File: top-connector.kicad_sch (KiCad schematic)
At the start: 6 parts, among them J1 Compute-Module-4_Plug_Connect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, Q2 PJE138K

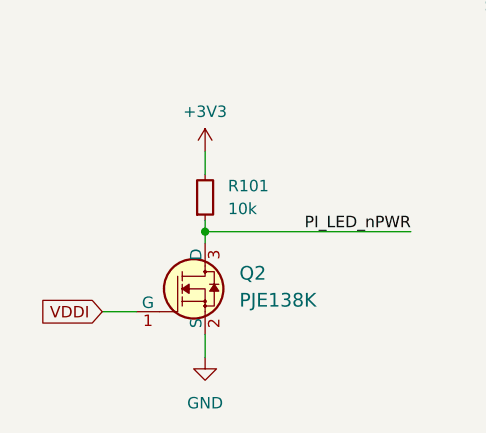
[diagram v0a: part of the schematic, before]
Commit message: [#57505] Continue migration to hierarchical schematic
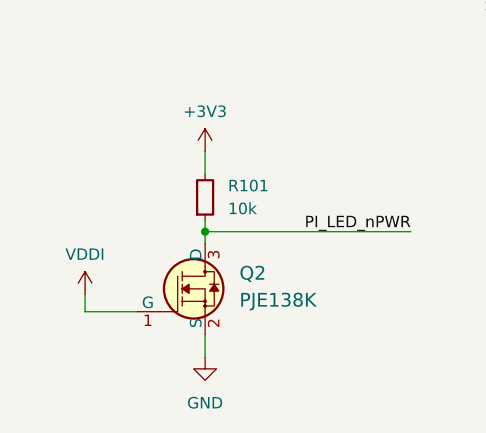
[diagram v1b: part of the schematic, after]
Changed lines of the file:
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@@
+    (stroke (width 0) (type default))
+  )
+  (wire (pts (xy 33.655 156.845) (xy 33.655 158.75))
     (stroke (width 0) (type default))
   )
@@
     (stroke (width 0) (type default))
   )
-  (wire (pts (xy 35.56 158.75) (xy 39.37 158.75))
+  (wire (pts (xy 33.655 158.75) (xy 39.37 158.75))
     (stroke (width 0) (type default))
   )
@@
     (effects (font (size 1.27 1.27)) (justify right))
     (property "Intersheetrefs" "${INTERSHEET_REFS}" (at 96.0421 76.1206 0)
-      (effects (font (size 1.27 1.27)) (justify right))
-    )
-  )
-  (global_label "VDDI" (shape input) (at 35.56 158.75 180) (fields_autoplaced)
-    (effects (font (size 1.27 1.27)) (justify right))
-    (property "Intersheetrefs" "${INTERSHEET_REFS}" (at 28.3414 158.75 0)
       (effects (font (size 1.27 1.27)) (justify right))
     )
@@
         )
       )
+    )
+  )
+  (symbol (lib_id "antmicropower:VDDI") (at 33.655 156.845 0) (unit 1)
+    (in_bom yes) (on_board yes) (dnp no) (fields_autoplaced)
+    (property "Reference" "#PWR0323" (at 33.655 160.655 0)
+      (effects (font (size 1.27 1.27)) hide)
+    )
+    (property "Value" "VDDI" (at 33.655 152.4 0)
+      (effects (font (size 1.27 1.27)))
+    )
+    (property "Footprint" "" (at 33.655 156.845 0)
+      (effects (font (size 1.27 1.27)) hide)
+    )
+    (property "Datasheet" "" (at 33.655 156.845 0)
+      (effects (font (size 1.27 1.27)) hide)
+    )
+    (pin "1")
+    (instances
+      (project "polarfire-som"
+        (path "/db4a0d3e-2eb3-499e-977d-6eb378cfd3ed/debae449-a92d-4184-817e-09f6daf3da7c"
+          (reference "#PWR0323") (unit 1)
+        )
+      )

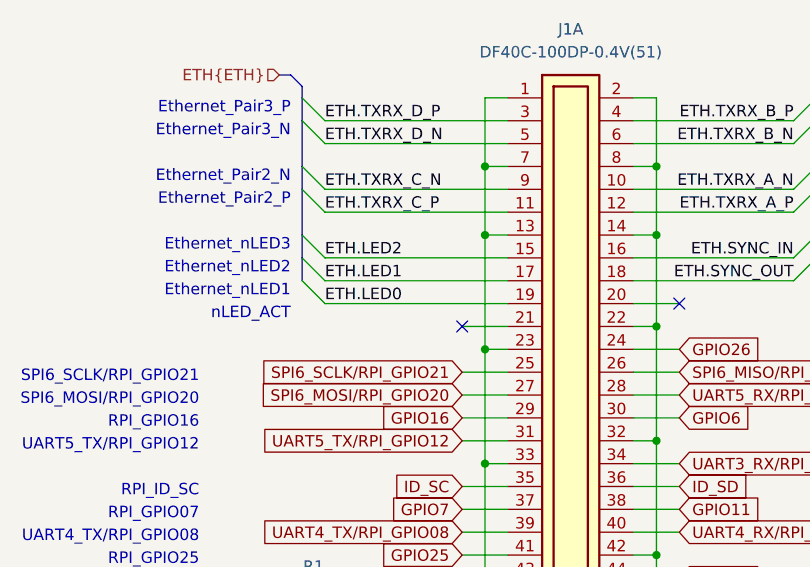
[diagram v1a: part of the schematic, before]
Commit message: [#57422] Add ETH PHY strap, WL_BT UART level shifter, fiducials, remove BYP_EN
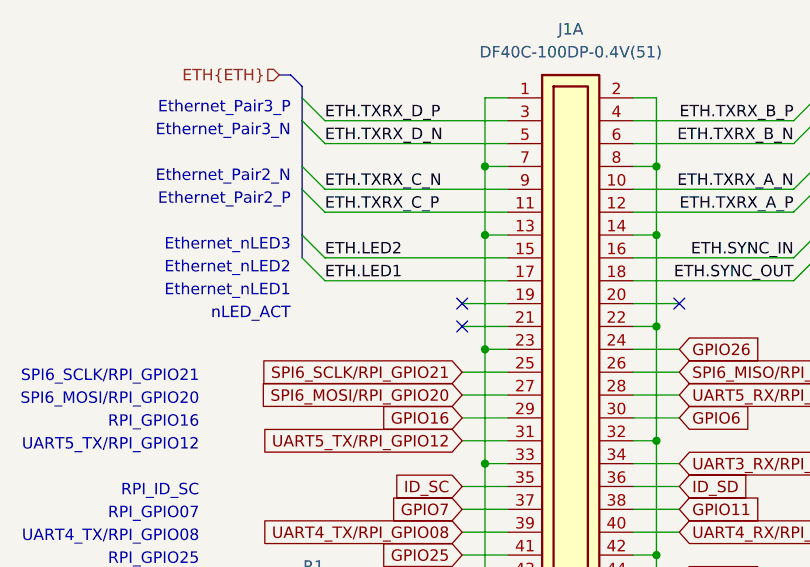
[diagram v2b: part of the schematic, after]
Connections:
- net ETH.LED0: no longer names the net of J1.19
- no-connect marks 9 -> 10
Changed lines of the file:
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@@
   (no_connect (at 104.14 55.88))
   (no_connect (at 123.19 124.46))
+  (no_connect (at 104.14 53.34))
   (no_connect (at 123.19 154.94))
   (no_connect (at 128.27 53.34))
@@
     (stroke (width 0) (type default))
   )
-  (bus_entry (at 86.36 50.8) (size 2.54 2.54)
-    (stroke (width 0) (type default))
-  )
   (bus_entry (at 41.148 99.06) (size 2.54 2.54)
     (stroke (width 0) (type default))
@@
     (stroke (width 0) (type default))
   )
+  (wire (pts (xy 104.14 53.34) (xy 109.22 53.34))
+    (stroke (width 0) (type default))
+  )
   (wire (pts (xy 104.14 63.5) (xy 109.22 63.5))
     (stroke (width 0) (type default))
@@
     (stroke (width 0) (type default))
   )
-  (bus (pts (xy 86.36 48.26) (xy 86.36 50.8))
-    (stroke (width 0) (type default))
-  )
   (wire (pts (xy 106.68 45.72) (xy 106.68 58.42))
     (stroke (width 0) (type default))
@@
     (stroke (width 0) (type default))
   )
-  (wire (pts (xy 88.9 53.34) (xy 109.22 53.34))
-    (stroke (width 0) (type default))
-  )
   (wire (pts (xy 104.14 133.35) (xy 104.14 134.62))
     (stroke (width 0) (type default))
@@
     (effects (font (size 1.27 1.27)) (justify right bottom))
   )
-  (label "ETH.LED0" (at 88.9 53.34 0) (fields_autoplaced)
-    (effects (font (size 1.27 1.27)) (justify left bottom))
-  )
   (label "ETH.LED1" (at 88.9 50.8 0) (fields_autoplaced)

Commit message: [#57505] Finish defining buses
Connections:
- net ID_SC renamed ID.SCL
- net ID_SD renamed ID.SDA
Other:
- moved on the sheet: J1A, Q2, R1, R101, R13, R15

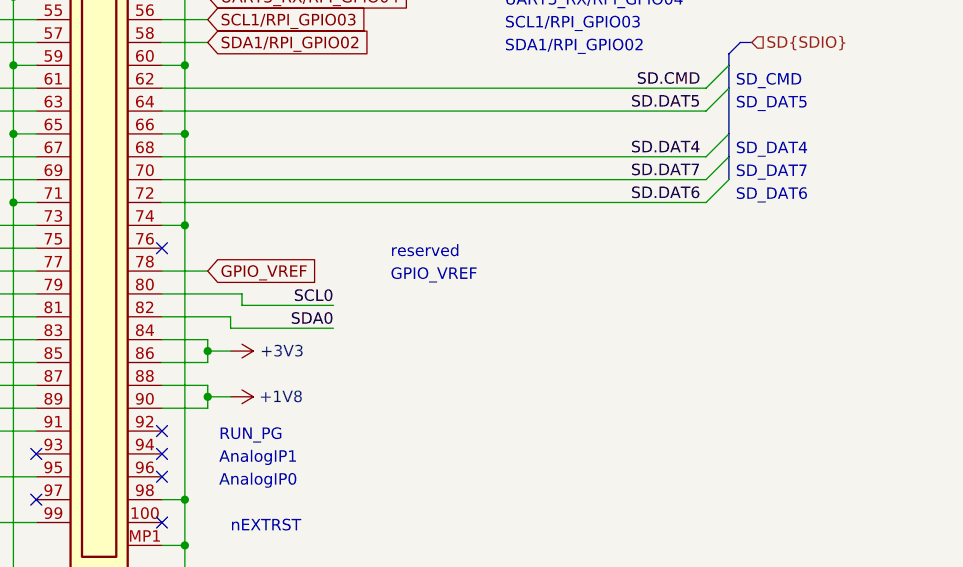
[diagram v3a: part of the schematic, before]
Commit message: [#57505] Start moving logic level converters to GPIO sheet
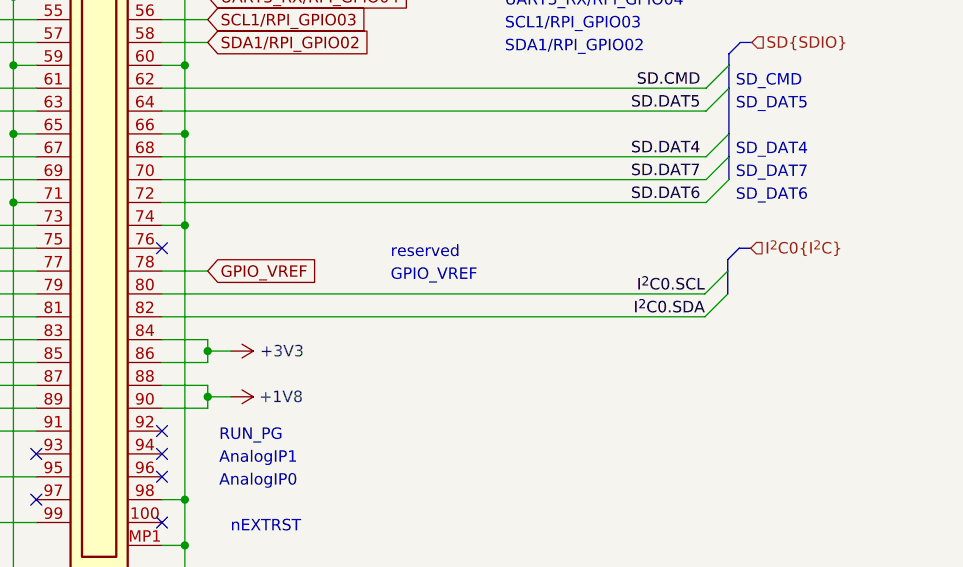
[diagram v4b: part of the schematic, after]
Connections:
- net SCL0 renamed I^{2}C0.SCL
- net SDA0 renamed I^{2}C0.SDA
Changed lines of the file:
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@@
+    (stroke (width 0) (type default))
+  )
+  (bus_entry (at 277.495 175.895) (size -2.54 2.54)
     (stroke (width 0) (type default))
   )
@@
     (stroke (width 0) (type default))
   )
+  (bus_entry (at 277.495 173.355) (size -2.54 2.54)
+    (stroke (width 0) (type default))
+  )
   (bus (pts (xy 177.8 92.075) (xy 177.8 94.615))
     (stroke (width 0) (type default))
@@
     (stroke (width 0) (type default))
   )
+  (bus (pts (xy 280.035 170.815) (xy 278.765 170.815))
+    (stroke (width 0) (type default))
+  )
   (wire (pts (xy 214.63 99.695) (xy 219.71 99.695))
     (stroke (width 0) (type default))
@@
     (stroke (width 0) (type default))
   )
-  (wire (pts (xy 222.25 179.705) (xy 233.68 179.705))
-    (stroke (width 0) (type default))
-  )
   (wire (pts (xy 195.58 186.055) (xy 200.66 186.055))
     (stroke (width 0) (type default))
@@
     (stroke (width 0) (type default))
   )
-  (wire (pts (xy 223.52 177.165) (xy 223.52 175.895))
-    (stroke (width 0) (type default))
-  )
   (wire (pts (xy 195.58 188.595) (xy 200.66 188.595))
     (stroke (width 0) (type default))
@@
     (stroke (width 0) (type default))
   )
-  (wire (pts (xy 223.52 175.895) (xy 214.63 175.895))
+  (wire (pts (xy 214.63 175.895) (xy 274.955 175.895))
     (stroke (width 0) (type default))
   )
@@
     (stroke (width 0) (type default))
   )
-  (wire (pts (xy 223.52 177.165) (xy 233.68 177.165))
-    (stroke (width 0) (type default))
-  )
   (bus (pts (xy 234.95 92.075) (xy 234.95 94.615))
     (stroke (width 0) (type default))
   )
+  (bus (pts (xy 277.495 172.085) (xy 277.495 173.355))
+    (stroke (width 0) (type default))
+  )
   (wire (pts (xy 219.71 187.325) (xy 219.71 186.055))
     (stroke (width 0) (type default))
@@
     (stroke (width 0) (type default))
   )
-  (wire (pts (xy 222.25 179.705) (xy 222.25 178.435))
-    (stroke (width 0) (type default))
-  )
   (wire (pts (xy 200.66 76.835) (xy 198.12 76.835))
     (stroke (width 0) (type default))
@@
     (stroke (width 0) (type default))
   )
+  (bus (pts (xy 277.495 173.355) (xy 277.495 175.895))
+    (stroke (width 0) (type default))
+  )
   (bus (pts (xy 127.635 142.875) (xy 126.365 142.875))
     (stroke (width 0) (type default))
@@
     (stroke (width 0) (type default))
   )
+  (bus (pts (xy 278.765 170.815) (xy 277.495 172.085))
+    (stroke (width 0) (type default))
+  )
   (wire (pts (xy 214.63 89.535) (xy 232.41 89.535))
     (stroke (width 0) (type default))
@@
     (stroke (width 0) (type default))
   )
-  (wire (pts (xy 222.25 178.435) (xy 214.63 178.435))
+  (wire (pts (xy 214.63 178.435) (xy 274.955 178.435))
     (stroke (width 0) (type default))
   )
@@
     (effects (font (size 1.27 1.27)) (justify right bottom))
   )
+  (label "I^{2}C0.SCL" (at 274.955 175.895 180) (fields_autoplaced)
+    (effects (font (size 1.27 1.27)) (justify right bottom))
+  )
   (label "ETH.TXRX_B_N" (at 232.41 81.915 180) (fields_autoplaced)
     (effects (font (size 1.27 1.27)) (justify right bottom))
@@
     (effects (font (size 1.27 1.27)) (justify left bottom))
   )
-  (label "SCL0" (at 233.68 177.165 180) (fields_autoplaced)
-    (effects (font (size 1.27 1.27)) (justify right bottom))
-  )
   (label "PI_LED_nPWR" (at 161.29 196.215 180) (fields_autoplaced)
     (effects (font (size 1.27 1.27)) (justify right bottom))
@@
     (effects (font (size 1.27 1.27)) (justify left bottom))
   )
-  (label "SDA0" (at 233.68 179.705 180) (fields_autoplaced)
-    (effects (font (size 1.27 1.27)) (justify right bottom))
-  )
   (label "SD.DAT2" (at 132.08 163.195 0) (fields_autoplaced)
     (effects (font (size 1.27 1.27)) (justify left bottom))
@@
     (effects (font (size 1.27 1.27)) (justify right bottom))
   )
+  (label "I^{2}C0.SDA" (at 274.955 178.435 180) (fields_autoplaced)
+    (effects (font (size 1.27 1.27)) (justify right bottom))
+  )
   (global_label "SPI6_SCLK{slash}RPI_GPIO21" (shape input) (at 195.58 107.315 180) (fields_autoplaced)
     (effects (font (size 1.27 1.27)) (justify right))
@@
     (effects (font (size 1.27 1.27)) (justify left))
   )
+  (hierarchical_label "I^{2}C0{I^{2}C}" (shape input) (at 280.035 170.815 0) (fields_autoplaced)
+    (effects (font (size 1.27 1.27)) (justify left))
+  )

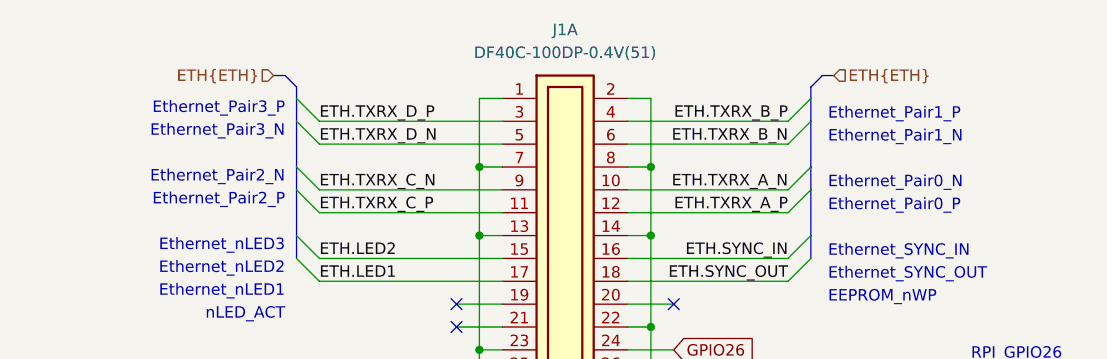
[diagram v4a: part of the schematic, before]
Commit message: [#57505] Finish migration to hierarchical structure
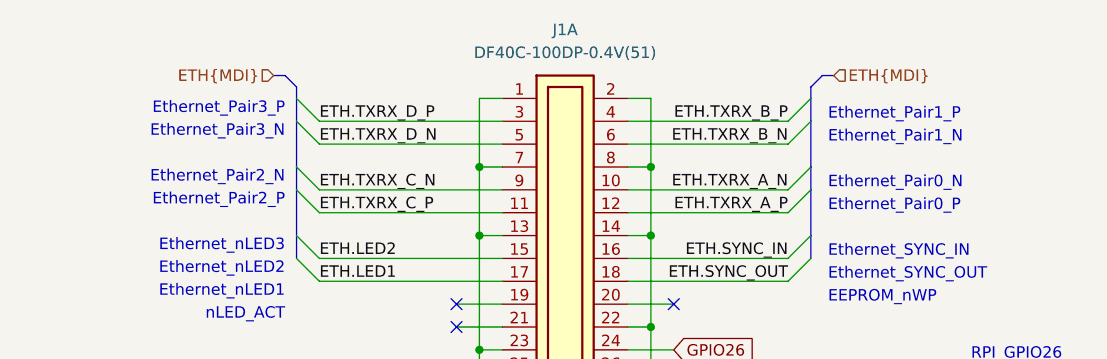
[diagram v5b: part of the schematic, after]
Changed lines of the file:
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@@
     (comment 1 "www.antmicro.com")
   )
-  (bus_alias "ETH" (members "TXRX_A_P" "TXRX_A_N" "TXRX_B_P" "TXRX_B_N" "TXRX_C_P" "TXRX_C_N" "TXRX_D_P" "TXRX_D_N" "LED[0..2]" "SYNC_IN" "SYNC_OUT"))
   (bus_alias "I^{2}C" (members "SDA" "SCL"))
+  (bus_alias "MDI" (members "TXRX_A_P" "TXRX_A_N" "TXRX_B_P" "TXRX_B_N" "TXRX_C_P" "TXRX_C_N" "TXRX_D_P" "TXRX_D_N" "LED[0..2]" "SYNC_IN" "SYNC_OUT"))
   (bus_alias "SDIO" (members "DAT[0..7]" "CMD" "CLK" "STRB" "RST_n"))
   (junction (at 217.17 127.635) (diameter 0) (color 0 0 0 0)
@@
     (effects (font (size 1.27 1.27)) (justify left))
   )
-  (hierarchical_label "ETH{ETH}" (shape input) (at 175.26 74.295 180) (fields_autoplaced)
-    (effects (font (size 1.27 1.27)) (justify right))
-  )
-  (hierarchical_label "ETH{ETH}" (shape input) (at 237.49 74.295 0) (fields_autoplaced)
-    (effects (font (size 1.27 1.27)) (justify left))
-  )
+  (hierarchical_label "ETH{MDI}" (shape input) (at 175.26 74.295 180) (fields_autoplaced)
+    (effects (font (size 1.27 1.27)) (justify right))
+  )
+  (hierarchical_label "ETH{MDI}" (shape input) (at 237.49 74.295 0) (fields_autoplaced)
+    (effects (font (size 1.27 1.27)) (justify left))
+  )

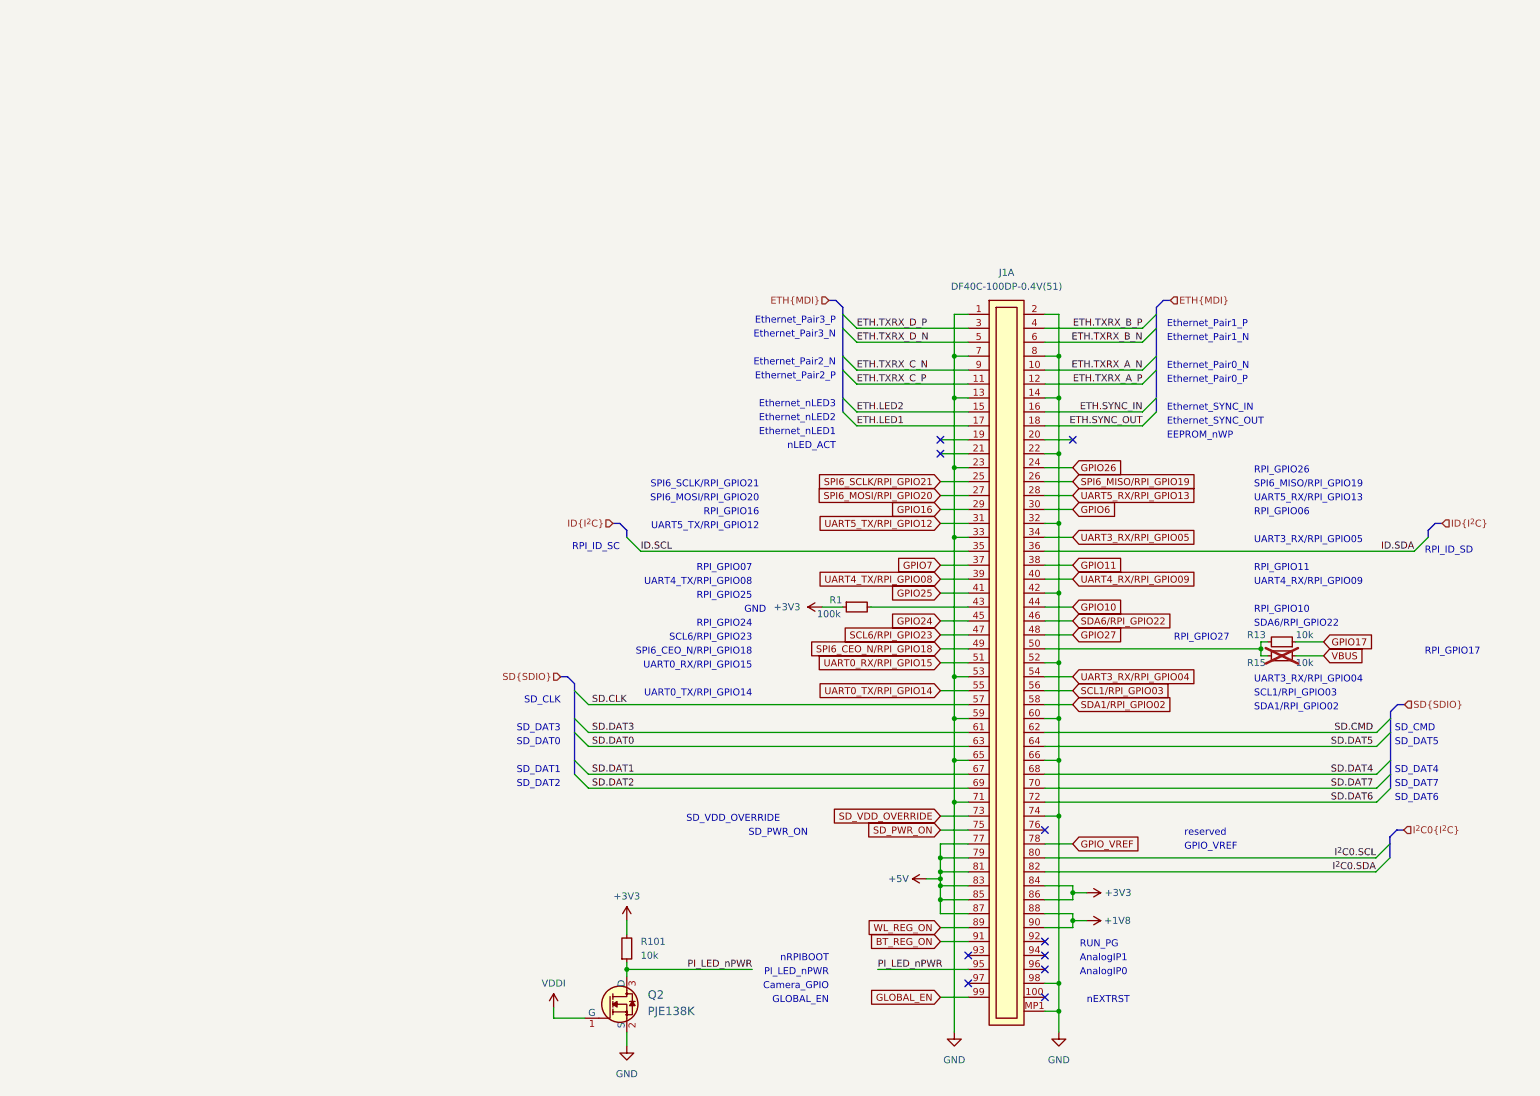
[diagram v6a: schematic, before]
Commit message: [#57422] Align schematics
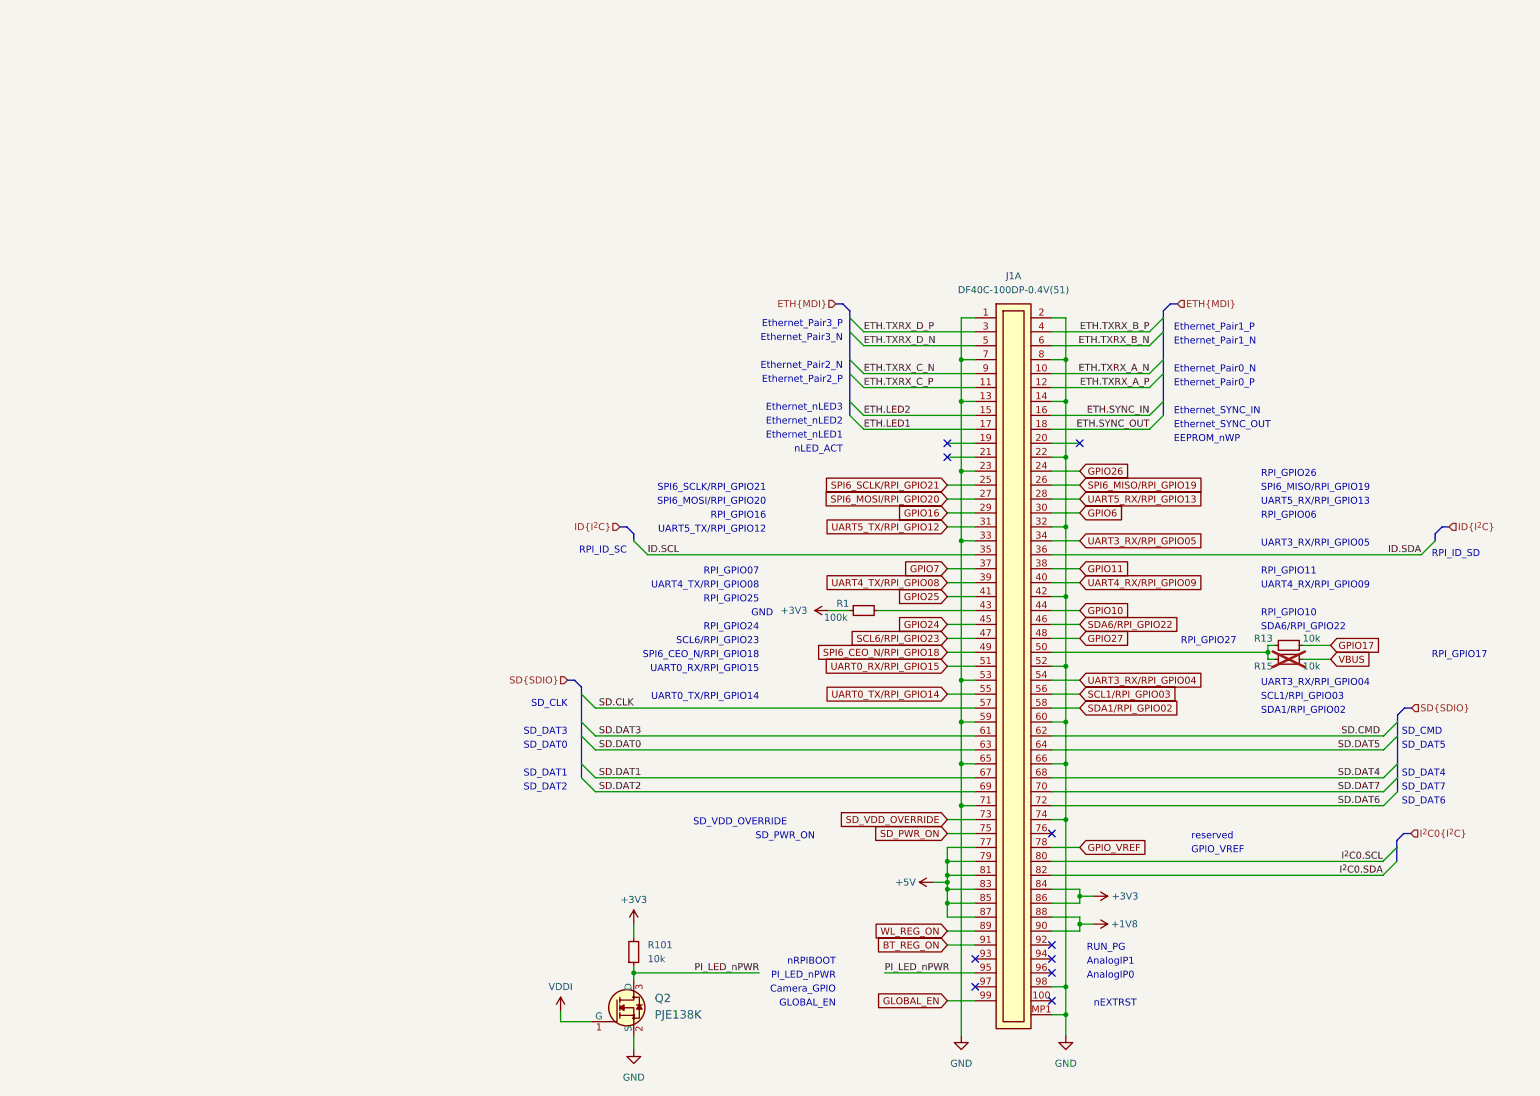
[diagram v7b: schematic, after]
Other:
- moved on the sheet: J1A, Q2, R1, R101, R13, R15
